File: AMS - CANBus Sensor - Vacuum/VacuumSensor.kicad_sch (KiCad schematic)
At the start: 3 parts, among them IC4 24PCDFA6D, IC5 INA849DR

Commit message: i think the Vacuum sensor is done i need to test s afew things and then this is ready for fab
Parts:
- removed IC5: INA849DR, Samac_Sys:SOIC127P600X175-8N, symbol SamacSys_Parts:INA849DR
- removed R10: YR1B665RCC, Samac_Sys:RESAD1550W60L630D230, symbol SamacSys_Parts:YR1B665RCC
- added IC8: INA849DR, SOIC127P600X175-8N, symbol SamacSys_Parts:INA849DR
- added R14: YR1B665RCC, RESAD1550W60L630D230, symbol SamacSys_Parts:YR1B665RCC
- IC4: footprint Samac_Sys:24PCDFA6D -> SamacSys_Parts:24PCDFA6D
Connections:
- net 2.5V: now also IC8.6 (REF)
- net 5V: now also IC8.8 (+VS)
- net GND: now also IC8.5 (-VS)
- net VoutToADC: now also IC8.7 (OUT)
- net at IC4.4 (OUTPUT_B): now also IC8.1 (-IN)
- net at IC4.2 (OUTPUT_A): now also IC8.4 (+IN)
- new net: IC8.2 (RG_1), R14.1
- new net: IC8.3 (RG_2), R14.2
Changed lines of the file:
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@@
 	)
 	(symbol
-		(lib_id "SamacSys_Parts:INA849DR")
-		(at 138.43 80.01 0)
-		(unit 1)
-		(exclude_from_sim no)
-		(in_bom yes)
-		(on_board yes)
-		(dnp no)
-		(property "Reference" "IC5"
-			(at 152.4 73.279 0)
-			(effects
-				(font
-					(size 1.27 1.27)
-				)
-			)
-		)
-		(property "Value" "INA849DR"
-			(at 152.4 75.5904 0)
-			(effects
-				(font
-					(size 1.27 1.27)
-				)
-			)
-		)
-		(property "Footprint" "Samac_Sys:SOIC127P600X175-8N"
-			(at 162.56 77.47 0)
-			(effects
-				(font
-					(size 1.27 1.27)
-				)
-				(justify left)
-				(hide yes)
-			)
-		)
-		(property "Datasheet" "https://www.ti.com/lit/ds/symlink/ina849.pdf?ts=1609495728489&ref_url=https%253A%252F%252Fwww.ti.com%252Fproduct%252FINA849"
-			(at 162.56 80.01 0)
-			(effects
-				(font
-					(size 1.27 1.27)
-				)
-				(justify left)
-				(hide yes)
-			)
-		)
-		(property "Description" "Texas Instruments Ultra-low noise (1 nV/vHz), high-speed (28 MHz, 35 V/), precision (35 V) instrumentation amplifier"
-			(at 162.56 82.55 0)
-			(effects
-				(font
-					(size 1.27 1.27)
-				)
-				(justify left)
-				(hide yes)
-			)
-		)
-		(property "Height" "1.75"
-			(at 162.56 85.09 0)
-			(effects
-				(font
-					(size 1.27 1.27)
-				)
-				(justify left)
-				(hide yes)
-			)
-		)
-		(property "Mouser Part Number" "595-INA849DR"
-			(at 162.56 87.63 0)
-			(effects
-				(font
-					(size 1.27 1.27)
-				)
-				(justify left)
-				(hide yes)
-			)
-		)
-		(property "Mouser Price/Stock" "https://www.mouser.co.uk/ProductDetail/Texas-Instruments/INA849DR?qs=eP2BKZSCXI4qgDpsz1tg9g%3D%3D"
-			(at 162.56 90.17 0)
-			(effects
-				(font
-					(size 1.27 1.27)
-				)
-				(justify left)
-				(hide yes)
-			)
-		)
-		(property "Manufacturer_Name" "Texas Instruments"
-			(at 162.56 92.71 0)
-			(effects
-				(font
-					(size 1.27 1.27)
-				)
-				(justify left)
-				(hide yes)
-			)
-		)
-		(property "Manufacturer_Part_Number" "INA849DR"
-			(at 162.56 95.25 0)
-			(effects
-				(font
-					(size 1.27 1.27)
-				)
-				(justify left)
-				(hide yes)
-			)
-		)
-		(pin "1"
-		)
-		(pin "2"
-		)
-		(pin "3"
-		)
-		(pin "4"
-		)
-		(pin "5"
-		)
-		(pin "6"
-		)
-		(pin "7"
-		)
-		(pin "8"
-		)
-		(instances
-			(project "AMS - CANBus Sensor - Vacuum"
-				(path "/1c8b441e-37da-469b-a62d-a2093a833f7a/078480f7-efd8-4daf-8b91-3ac2141f17a0"
-					(reference "IC5")
-					(unit 1)
-				)
-				(path "/1c8b441e-37da-469b-a62d-a2093a833f7a/f37fe740-c6f5-4b65-ba1e-97939b966df4"
-					(reference "IC7")
-					(unit 1)
-				)
-			)
-		)
-	)
-	(symbol
+		(lib_name "YR1B665RCC_1")
 		(lib_id "SamacSys_Parts:YR1B665RCC")
 		(at 81.28 90.17 0)
@@
 		(on_board yes)
 		(dnp no)
-		(property "Reference" "R10"
-			(at 90.17 84.455 0)
+		(fields_autoplaced yes)
+		(property "Reference" "R14"
+			(at 90.17 83.82 0)
 			(effects
 				(font
@@
 		)
 		(property "Value" "YR1B665RCC"
-			(at 90.17 86.7664 0)
-			(effects
-				(font
-					(size 1.27 1.27)
-				)
-			)
-		)
-		(property "Footprint" "Samac_Sys:RESAD1550W60L630D230"
+			(at 90.17 86.36 0)
+			(effects
+				(font
+					(size 1.27 1.27)
+				)
+			)
+		)
+		(property "Footprint" "RESAD1550W60L630D230"
 			(at 95.25 88.9 0)
 			(effects
@@
 			)
 		)
-		(property "Datasheet" "https://componentsearchengine.com/Datasheets/1/YR1B665RCC.pdf"
+		(property "Datasheet" "https://www.te.com/commerce/DocumentDelivery/DDEController?Action=srchrtrv&DocNm=1309350_PASSIVE_COMPONENT&DocType=Catalog%20Section&DocLang=English&PartCntxt=8-1676914-2&DocFormat=pdf"
 			(at 95.25 91.44 0)
 			(effects
@@
 			)
 		)
-		(property "Description" "TE Connectivity R Series Axial Through Hole Fixed Resistor 665 +/-0.1% 0.25W +/-15ppm/C"
+		(property "Description" "Body Features: Lead Type Axial-Leaded | Configuration Features: Number of Resistors 1 | Dimensions: Passive Component Dimensions 6.3 x 2.3 MM | Electrical Characteristics: Passive Component Tolerance .1 PCT | Power Rating .25 WATT | Operating Voltage 250 V | Resistance Value 665 OHM | Resistance Class Up to 1k | Packaging Features: Packaging Method Ammo Packed | Product Type Features: Element Type Thin Film | Resistor Type Precision Resistor | Termination Features: Termination Area Base Material Copper |"
 			(at 95.25 93.98 0)
 			(effects
@@
 			)
 		)
-		(property "Mouser Price/Stock" "https://www.mouser.com/Search/Refine.aspx?Keyword=279-YR1B665RCC"
+		(property "Mouser Price/Stock" "https://www.mouser.co.uk/ProductDetail/TE-Connectivity-Holsworthy/YR1B665RCC?qs=8G8kQhBkhGiPCBHktkhxCA%3D%3D"
 			(at 95.25 101.6 0)
 			(effects
@@
 			(project "AMS - CANBus Sensor - Vacuum"
 				(path "/1c8b441e-37da-469b-a62d-a2093a833f7a/078480f7-efd8-4daf-8b91-3ac2141f17a0"
-					(reference "R10")
+					(reference "R14")
 					(unit 1)
 				)
 				(path "/1c8b441e-37da-469b-a62d-a2093a833f7a/f37fe740-c6f5-4b65-ba1e-97939b966df4"
-					(reference "R11")
+					(reference "R15")
 					(unit 1)
 				)
@@
 			)
 		)
-		(property "Footprint" "Samac_Sys:24PCDFA6D"
+		(property "Footprint" "SamacSys_Parts:24PCDFA6D"
 			(at 60.96 66.04 0)
 			(effects
@@
 					(unit 1)
 				)
+			)
+		)
+	)
+	(symbol
+		(lib_name "INA849DR_1")
+		(lib_id "SamacSys_Parts:INA849DR")
+		(at 138.43 80.01 0)
+		(unit 1)
+		(exclude_from_sim no)
+		(in_bom yes)
+		(on_board yes)
+		(dnp no)
+		(fields_autoplaced yes)
+		(property "Reference" "IC8"
+			(at 152.4 72.39 0)
+			(effects
+				(font
+					(size 1.27 1.27)
+				)
+			)
+		)
+		(property "Value" "INA849DR"
+			(at 152.4 74.93 0)
+			(effects
+				(font
+					(size 1.27 1.27)
+				)
+			)
+		)
+		(property "Footprint" "SOIC127P600X175-8N"
+			(at 162.56 77.47 0)
+			(effects
+				(font
+					(size 1.27 1.27)
+				)
+				(justify left)
+				(hide yes)
+			)
+		)
+		(property "Datasheet" "https://www.ti.com/lit/ds/symlink/ina849.pdf?ts=1609495728489&ref_url=https%253A%252F%252Fwww.ti.com%252Fproduct%252FINA849"
+			(at 162.56 80.01 0)
+			(effects
+				(font
+					(size 1.27 1.27)
+				)
+				(justify left)
+				(hide yes)
+			)
+		)
+		(property "Description" "Texas Instruments Ultra-low noise (1 nV/vHz), high-speed (28 MHz, 35 V/), precision (35 V) instrumentation amplifier"
+			(at 162.56 82.55 0)
+			(effects
+				(font
+					(size 1.27 1.27)
+				)
+				(justify left)
+				(hide yes)
+			)
+		)
+		(property "Height" "1.75"
+			(at 162.56 85.09 0)
+			(effects
+				(font
+					(size 1.27 1.27)
+				)
+				(justify left)
+				(hide yes)
+			)
+		)
+		(property "Mouser Part Number" "595-INA849DR"
+			(at 162.56 87.63 0)
+			(effects
+				(font
+					(size 1.27 1.27)
+				)
+				(justify left)
+				(hide yes)
+			)
+		)
+		(property "Mouser Price/Stock" "https://www.mouser.co.uk/ProductDetail/Texas-Instruments/INA849DR?qs=eP2BKZSCXI4qgDpsz1tg9g%3D%3D"
+			(at 162.56 90.17 0)
+			(effects
+				(font
+					(size 1.27 1.27)
+				)
+				(justify left)
+				(hide yes)
+			)
+		)
+		(property "Manufacturer_Name" "Texas Instruments"
+			(at 162.56 92.71 0)
+			(effects
+				(font
+					(size 1.27 1.27)
+				)
+				(justify left)
+				(hide yes)
+			)
+		)
+		(property "Manufacturer_Part_Number" "INA849DR"
+			(at 162.56 95.25 0)
+			(effects
+				(font
+					(size 1.27 1.27)
+				)
+				(justify left)
+				(hide yes)
+			)
+		)
+		(pin "6"
+		)
+		(pin "3"
+		)
+		(pin "4"
+		)
+		(pin "8"
+		)
+		(pin "1"
+		)
+		(pin "2"
+		)
+		(pin "7"
+		)
+		(pin "5"
+		)
+		(instances
+			(project "AMS - CANBus Sensor - Vacuum"
+				(path "/1c8b441e-37da-469b-a62d-a2093a833f7a/078480f7-efd8-4daf-8b91-3ac2141f17a0"
+					(reference "IC8")
+					(unit 1)
+				)
+				(path "/1c8b441e-37da-469b-a62d-a2093a833f7a/f37fe740-c6f5-4b65-ba1e-97939b966df4"
+					(reference "IC9")
+					(unit 1)
+				)

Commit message: vacuum wip
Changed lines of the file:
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@@
-	(wire
-		(pts
-			(xy 87.63 67.31) (xy 87.63 60.96)
-		)
-		(stroke
-			(width 0)
-			(type default)
-		)
-	)
 	(wire
 		(pts
@@
 	(wire
 		(pts
-			(xy 87.63 60.96) (xy 85.09 60.96)
+			(xy 88.9 60.96) (xy 85.09 60.96)
 		)
 		(stroke
@@
 	(hierarchical_label "GND"
 		(shape input)
-		(at 87.63 67.31 0)
+		(at 88.9 60.96 0)
 		(fields_autoplaced yes)
 		(effects

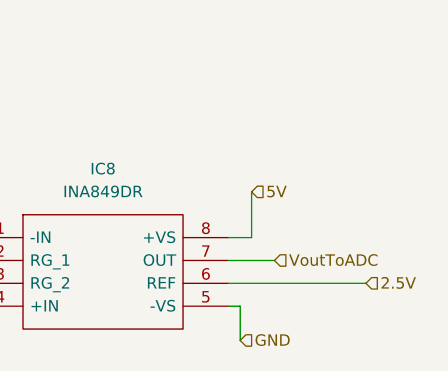
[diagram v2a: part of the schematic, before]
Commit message: Temperature Sensor board 1.0 REV. B
flipped the 3.3v and op amp to the back of the board to make assembly on a hotplate easier for the harder to place and solder components.
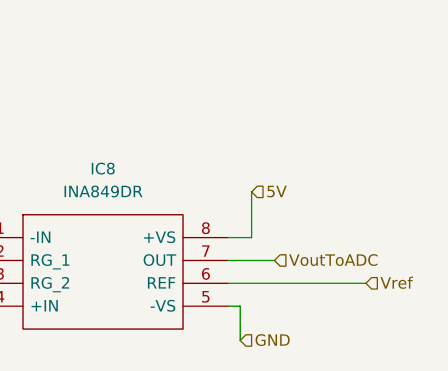
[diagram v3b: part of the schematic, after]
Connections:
- net 2.5V renamed Vref
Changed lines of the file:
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@@
 		)
 	)
-	(hierarchical_label "2.5V"
+	(hierarchical_label "Vref"
 		(shape input)
 		(at 181.61 85.09 0)

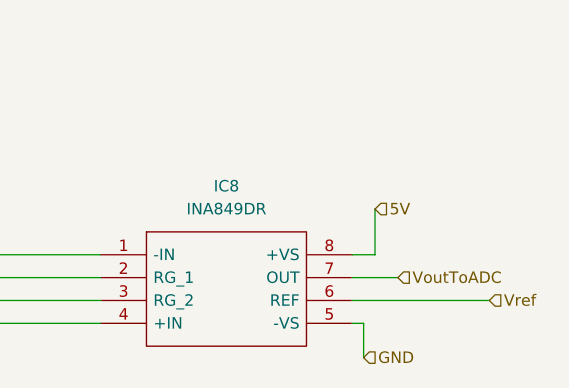
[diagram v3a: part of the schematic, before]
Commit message: swaping to a dual rail setup.
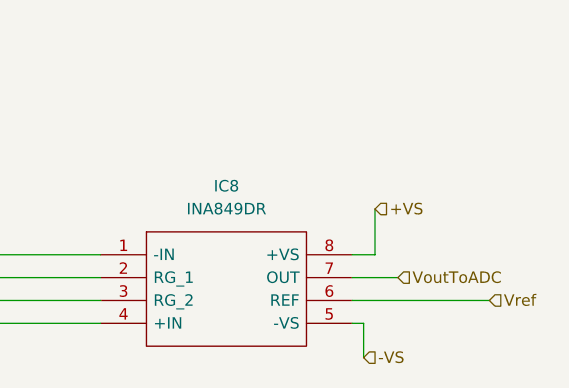
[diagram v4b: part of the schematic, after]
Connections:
- net GND: no longer IC8.5 (-VS)
- net 5V renamed +VS
- new net -VS: IC8.5 (-VS)
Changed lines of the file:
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@@
 		)
 	)
-	(hierarchical_label "5V"
+	(hierarchical_label "+VS"
 		(shape input)
 		(at 168.91 74.93 0)
@@
 		)
 	)
-	(hierarchical_label "GND"
+	(hierarchical_label "-VS"
 		(shape input)
 		(at 167.64 91.44 0)
